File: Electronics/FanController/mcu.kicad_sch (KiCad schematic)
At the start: 8 parts, among them SW1 RST_BUTTON, U4 STM32L051K8Tx, Y2 CM8V-T1A-32.768KHZ

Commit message: Started PCB-routing
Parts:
- C14: renamed from C8; footprint (none) -> Capacitor_SMD:C_1206_3216Metric_Pad1.33x1.80mm_HandSolder
- C15: renamed from C9; footprint (none) -> Capacitor_SMD:C_1206_3216Metric_Pad1.33x1.80mm_HandSolder
- C16: renamed from C10; footprint (none) -> Capacitor_SMD:C_1206_3216Metric_Pad1.33x1.80mm_HandSolder
- R14: renamed from R4; footprint (none) -> Resistor_SMD:R_1206_3216Metric_Pad1.30x1.75mm_HandSolder
- R15: renamed from R3; footprint (none) -> Resistor_SMD:R_1206_3216Metric_Pad1.30x1.75mm_HandSolder
- SW1: footprint (none) -> Button_Switch_SMD:SW_Push_1P1T-SH_NO_CK_KMR2xxG
- Y2: footprint CM8V32768TA020125 -> Crystal:Crystal_SMD_MicroCrystal_CC8V-T1A-2Pin_2.0x1.2mm_HandSoldering

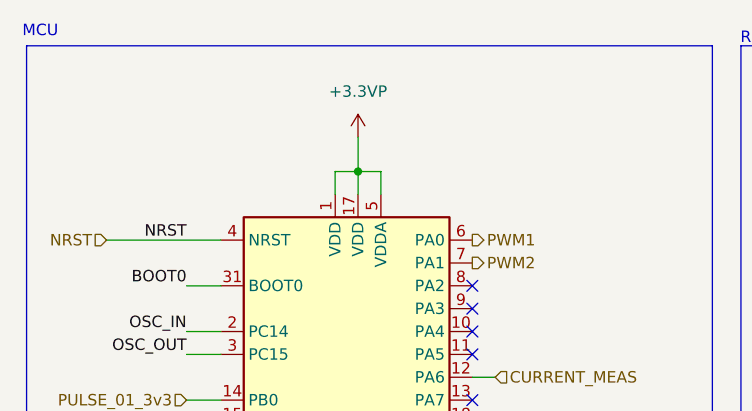
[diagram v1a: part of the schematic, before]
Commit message: Changed schematic
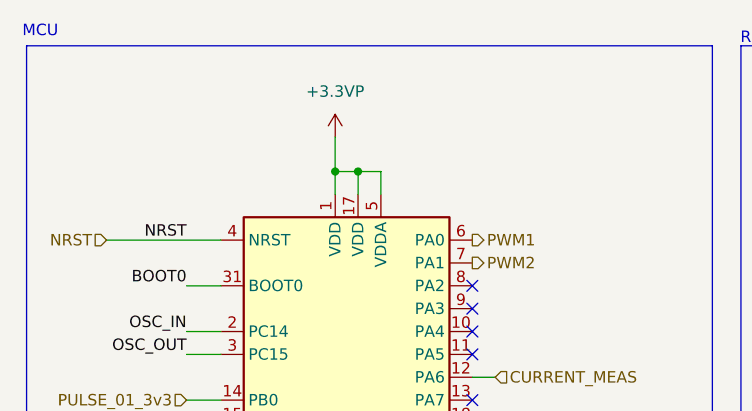
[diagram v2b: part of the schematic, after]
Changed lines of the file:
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@@
+	)
+	(junction
+		(at 74.93 48.26)
+		(diameter 0)
+		(color 0 0 0 0)
 	)
 	(junction
@@
 	(wire
 		(pts
+			(xy 74.93 48.26) (xy 77.47 48.26)
+		)
+		(stroke
+			(width 0)
+			(type default)
+		)
+	)
+	(wire
+		(pts
 			(xy 140.97 62.23) (xy 151.13 62.23)
 		)
@@
 	(wire
 		(pts
-			(xy 74.93 48.26) (xy 77.47 48.26)
-		)
-		(stroke
-			(width 0)
-			(type default)
-		)
-	)
-	(wire
-		(pts
-			(xy 77.47 44.45) (xy 77.47 48.26)
+			(xy 74.93 44.45) (xy 74.93 48.26)
 		)
 		(stroke
@@
 	(symbol
 		(lib_id "power:+3.3VP")
-		(at 77.47 44.45 0)
+		(at 74.93 44.45 0)
 		(unit 1)
 		(exclude_from_sim no)
@@
 		(fields_autoplaced yes)
 		(property "Reference" "#PWR033"
-			(at 81.28 45.72 0)
+			(at 78.74 45.72 0)
 			(effects
 				(font
@@
 		)
 		(property "Value" "+3.3VP"
-			(at 77.47 39.37 0)
+			(at 74.93 39.37 0)
 			(effects
 				(font
@@
 		)
 		(property "Footprint" ""
-			(at 77.47 44.45 0)
+			(at 74.93 44.45 0)
 			(effects
 				(font
@@
 		)
 		(property "Datasheet" ""
-			(at 77.47 44.45 0)
+			(at 74.93 44.45 0)
 			(effects
 				(font
@@
 		)
 		(property "Description" "Power symbol creates a global label with name \"+3.3VP\""
-			(at 77.47 44.45 0)
-			(effects
-				(font
+			(at 74.93 44.45 0)
+			(effects
+				(font

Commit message: Finished routing
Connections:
- net OSC_OUT: now also Y2.1 (X1); no longer Y2.
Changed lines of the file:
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@@
 		)
 		(property "Description" "CRYSTAL 32.768KHZ SMD"
-			(at 171.45 59.69 0)
+			(at 173.736 65.786 0)
 			(effects
 				(font
@@
 			)
 		)
-		(pin ""
+		(pin "1"
 		)
 		(pin "2"
